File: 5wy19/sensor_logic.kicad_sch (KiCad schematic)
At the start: 83 parts, among them Q1 BZX84Cxx, Q15 BCR183, Q16 BCR183, Q17 BC846, Q18 BC856, Q19 BAW56, Q2 BC846, Q20 BAW56, Q21 Unknown NFET, Q22 BAW56, Q5 BAW56, Q6 BAW56, Q8 BZX84Cxx, Q9 BC846

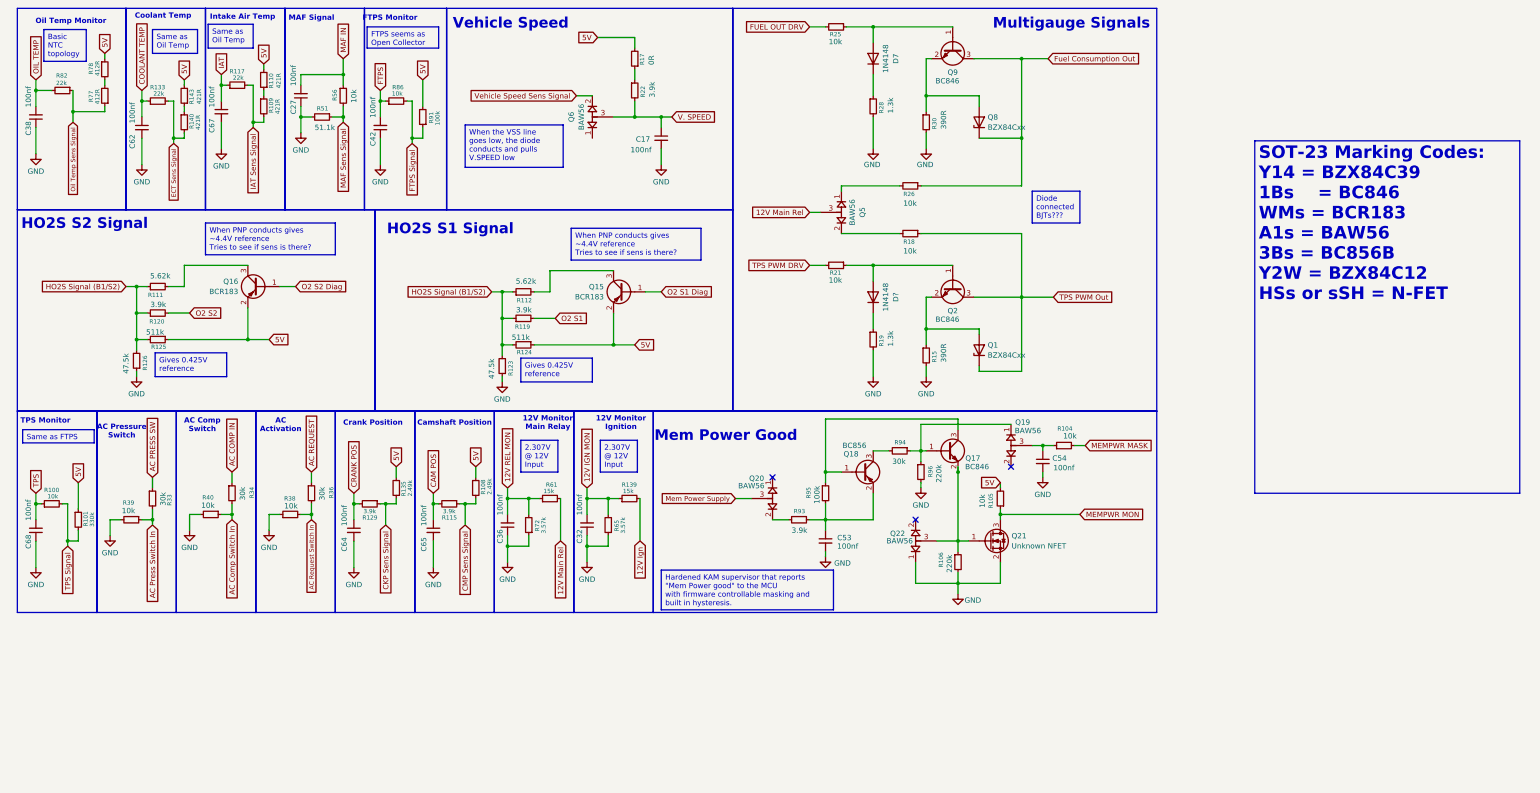
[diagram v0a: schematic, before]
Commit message: Finished most of the subsystems
-- MCU finished
-- Flash finished
-- Power Supply finished
-- I/O Drivers finished
-- CANBUS finished
-- Knock Control finished
-- Connector finished
-- Ignition Driver finished
-- Sensor Logic mostly finished
-- Logic ICs need some work
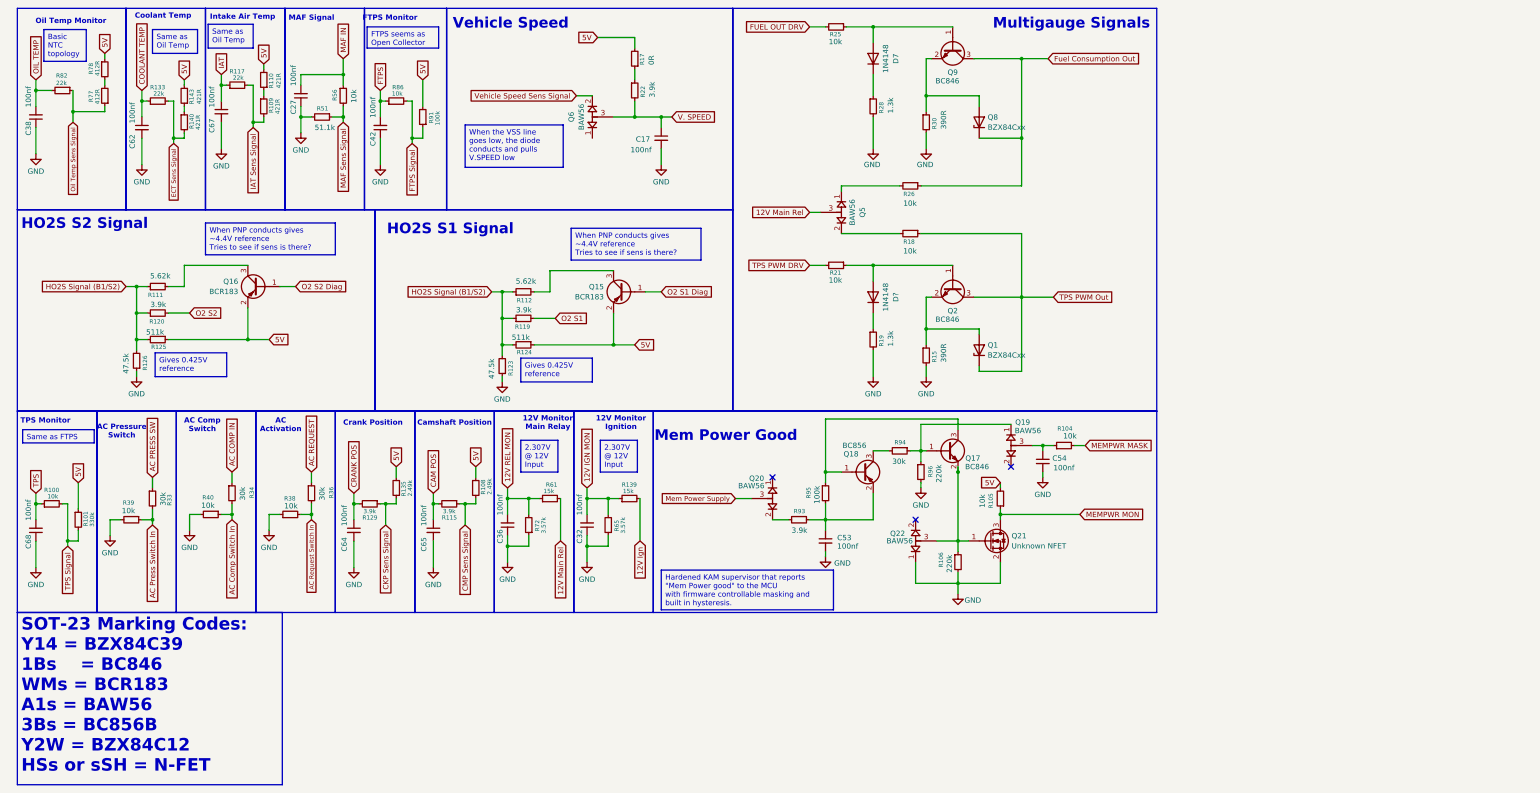
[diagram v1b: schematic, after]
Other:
- title: (none) -> SMIK43 5WY19 Rev. Eng
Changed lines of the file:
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@@
 	(generator_version "9.0")
 	(paper "A4")
+	(title_block
+		(title "SMIK43 5WY19 Rev. Eng")
+		(date "2025-10-28")
+		(rev "1.0")
+	)
 	(rectangle
 		(start 88.265 108.585)
@@
 	(text_box "SOT-23 Marking Codes:\nY14 = BZX84C39\n1Bs	= BC846\nWMs = BCR183\nA1s = BAW56\n3Bs = BC856B\nY2W = BZX84C12\nHSs or sSH = N-FET"
 		(exclude_from_sim no)
-		(at 308.61 43.815 0)
-		(size 63.5 84.455)
+		(at 12.065 156.845 0)
+		(size 63.5 41.275)
 		(margins 0.9525 0.9525 0.9525 0.9525)
 		(stroke
@@
 			)
 			(justify left top)
-		)
-	)
-	(text_box "Diode connected BJTs???"
-		(exclude_from_sim no)
-		(at 255.27 55.88 0)
-		(size 11.43 7.62)
-		(margins 0.9525 0.9525 0.9525 0.9525)
-		(stroke
-			(width 0)
-			(type solid)
-		)
-		(fill
-			(type none)
-		)
-		(effects
-			(font
-				(size 1.27 1.27)
-			)
-			(justify left top)

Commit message: Final schematic (except maybe some oversights)
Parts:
- added C48, C52, C59: 100nf, symbol Device:C_Small
- added R136, R137, R141, R142: 47.5k, symbol Device:R_Small
- gave numbers to parts that had none: 1
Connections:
- net 12V IGN MON: now also R139.2; no longer R139.1
- net 12V Ign: now also R139.1; no longer R139.2
- net 12V Main Rel: now also R61.1; no longer R61.2
- net 12V REL MON: now also R61.2; no longer R61.1
- net AC PRESS SW: now also R33.2; no longer R33.1
- net AC Press Switch In: now also R33.1; no longer R33.2
- net GND: now also C48.1, C59.1
- net HO2S Signal (B1/S2): no longer R112.1, R119.1, R123.2, R124.2
- net MAF IN: now also R56.2; no longer R56.1
- net MAF Sens Signal: now also R56.1; no longer R56.2
- new net HO2S Signal (B1/S1): R112.1, R119.1, R123.2, R124.2
- new net P5.12: R136.2, R142.2
- new net WHSP IN+: C52.1, C59.2, R137.2
- new net WHSP IN-: C48.2, C52.2, R141.2
- new net Wheel Speed Sens +: R136.1, R137.1
- new net Wheel Speed Sens -: R141.1, R142.1
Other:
- note added: "Wheel Speed Sensor"
- moved on the sheet: R139, R33, R56, R61
